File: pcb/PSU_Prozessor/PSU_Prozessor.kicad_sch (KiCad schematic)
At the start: 88 parts, among them IC1 6N138S, J1 ACJS-MHOP, J2 Conn_01x06, J3 FC68148S, J4 USB2066-05-RBHM-15-STB-00-01-A, J7 USB2066-05-RBHM-15-STB-00-01-A, Q1 BC847, Q2 2N7002, Q3 BC847, Q4 2N7002, Q5 BC847, Q6 2N7002, U1 TL072, U2 TL072

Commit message: New version with smaller enclosure
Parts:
- removed C23, C24, C27: 100n, Capacitor_SMD:C_1206_3216Metric_Pad1.33x1.80mm_HandSolder, symbol Device:C
- removed C25, C7: 1u, Capacitor_SMD:C_1206_3216Metric_Pad1.33x1.80mm_HandSolder, symbol Device:C
- removed H4, H5: MountingHole, KiCad_Libs:MountingHole_4mm, symbol Mechanical:MountingHole
- removed J4, J7: USB2066-05-RBHM-15-STB-00-01-A, SamacSys_Parts:USB206605RBHM15STB0001A, symbol SamacSys_Parts:USB2066-05-RBHM-15-STB-00-01-A
- removed J_Swtich_Lower2, J_Swtich_Upper2: Conn_01x08, Connector_JST:JST_PH_B8B-PH-K_1x08_P2.00mm_Vertical, symbol Connector_Generic:Conn_01x08
- removed Q3, Q5: BC847, Package_TO_SOT_SMD:SOT-23, symbol Transistor_BJT:BC847
- removed Q4, Q6: 2N7002, Package_TO_SOT_SMD:SOT-23, symbol Transistor_FET:2N7002
- removed R16, R6: 33k, Resistor_SMD:R_1206_3216Metric_Pad1.30x1.75mm_HandSolder, symbol Device:R
- removed R17, R7: 330, Resistor_SMD:R_1206_3216Metric_Pad1.30x1.75mm_HandSolder, symbol Device:R
- removed R18, R8: 10k, Resistor_SMD:R_1206_3216Metric_Pad1.30x1.75mm_HandSolder, symbol Device:R
- removed R21, R22, R23, R24: 0, Resistor_SMD:R_1206_3216Metric_Pad1.30x1.75mm_HandSolder, symbol Device:R
- removed U2: TL072, SamacSys_Parts:SOIC127P600X175-8N, symbol Amplifier_Operational:TL072
- removed XA1: Arduino_Due_Shield, Arduino:Arduino_Due_Shield, symbol arduino:Arduino_Due_Shield
- added C19: 100n, Capacitor_SMD:C_1206_3216Metric_Pad1.33x1.80mm_HandSolder, symbol Device:C
- added H3: MountingHole, KiCad_Libs:MountingHole_4mm, symbol Mechanical:MountingHole
- added XA1: Arduino_Nano_Socket, Arduino:Arduino_Nano_Socket, symbol arduino:Arduino_Nano_Socket
- renumbered C8 to C1, C21 to C10, C22 to C11, C16 to C12, C14 to C13, C17 to C14, C18 to C16, C19 to C17, C26 to C18, C10 to C2, C2 to C21, C3 to C22, C1 to C23, C12 to C3, C9 to C6, C11 to C7, C13 to C8, C6 to C9, H3 to H2, J3 to J1, J1 to J3, R19 to R1, R9 to R10, R1 to R12, R4 to R13, R2 to R14, R20 to R2, R14 to R3, R5 to R4, R12 to R5, R13 to R6, R15 to R7, R10 to R8, R3 to R9
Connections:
- net INT_Matrix is gone; now on net INT_Status: J_Main_Data1.10 (Pin_10)
- net RCLK_Lower is gone; now on net I2C_Reset: J_Swtich_Lower1.2 (Pin_2)
- net RCLK_Upper is gone; now on net I2C_Reset: J_Swtich_Upper1.2 (Pin_2)
- net SER_Lower is gone; now on net SCL: J_Swtich_Lower1.5 (Pin_5)
- net SER_Upper is gone; now on net SCL: J_Swtich_Upper1.5 (Pin_5)
- net SRCLK_Lower is gone; now on net SDA: J_Swtich_Lower1.4 (Pin_4)
- net SRCLK_Upper is gone; now on net SDA: J_Swtich_Upper1.4 (Pin_4)
- net SRCLR_Upper is gone; now on net INT_Switch: J_Swtich_Upper1.3 (Pin_3)
- net Vref_status is gone; now on net Vref_bl: J_Status1.6 (Pin_6)
- net CS_Amp_N: now also XA1.D6
- net CS_Display: now also XA1.D10 (D10_CS)
- net CS_Fram: now also XA1.D9
- net Expr_1: now also XA1.A0
- net Expr_2: now also XA1.A1
- net GND: now also U1.5 (+), C19.2, XA1.GND1 (GND), XA1.GND2 (GND)
- net I2C_Reset: now also XA1.D5
- net ID_Select_Display: now also XA1.D8
- net INT_Status: now also XA1.D3 (D3_INT1)
- net MISO: now also XA1.D12 (D12_MISO)
- net MOSI: now also J_Main_Data1.6 (Pin_6), XA1.D11 (D11_MOSI)
- net MidiIn: now also XA1.D0 (D0_RX0)
- net MidiOut: now also XA1.D1 (D1_TX0)
- net RCLK_MATRIX: now also XA1.A2
- net Reset_Display: now also XA1.D7
- net SCK: now also J_Main_Data1.7 (Pin_7), XA1.D13 (D13_SCK)
- net SCL: now also XA1.A5 (A5_SCL)
- net SDA: now also XA1.A4 (A4_SDA)
- net SEL_Matrix: now also XA1.A3
- net SW_Ext1: now also XA1.A6
- net SW_Ext2: now also XA1.A7
- net VDD3V3: now also XA1.AREF
- net VDD9V0: now also XA1.VIN
- net Vref_bl: now also J_Swtich_Lower1.6 (Pin_6), J_Swtich_Upper1.6 (Pin_6)
- net Vref_bl_pwm: now also XA1.D4
- net at U1.6 (-): now also U1.7
- net EN_SPL_Matrix: no longer names the net of J_Main_Data1.3 (Pin_3)
- net SRCLR_Lower renamed INT_Switch
- net INT_Switch: now also C19.1, XA1.D2 (D2_INT0)
- removed net Vref_ge: J_Swtich_Lower1.6 (Pin_6), J_Swtich_Upper1.6 (Pin_6), U1.7
- no-connect marks 56 -> 20

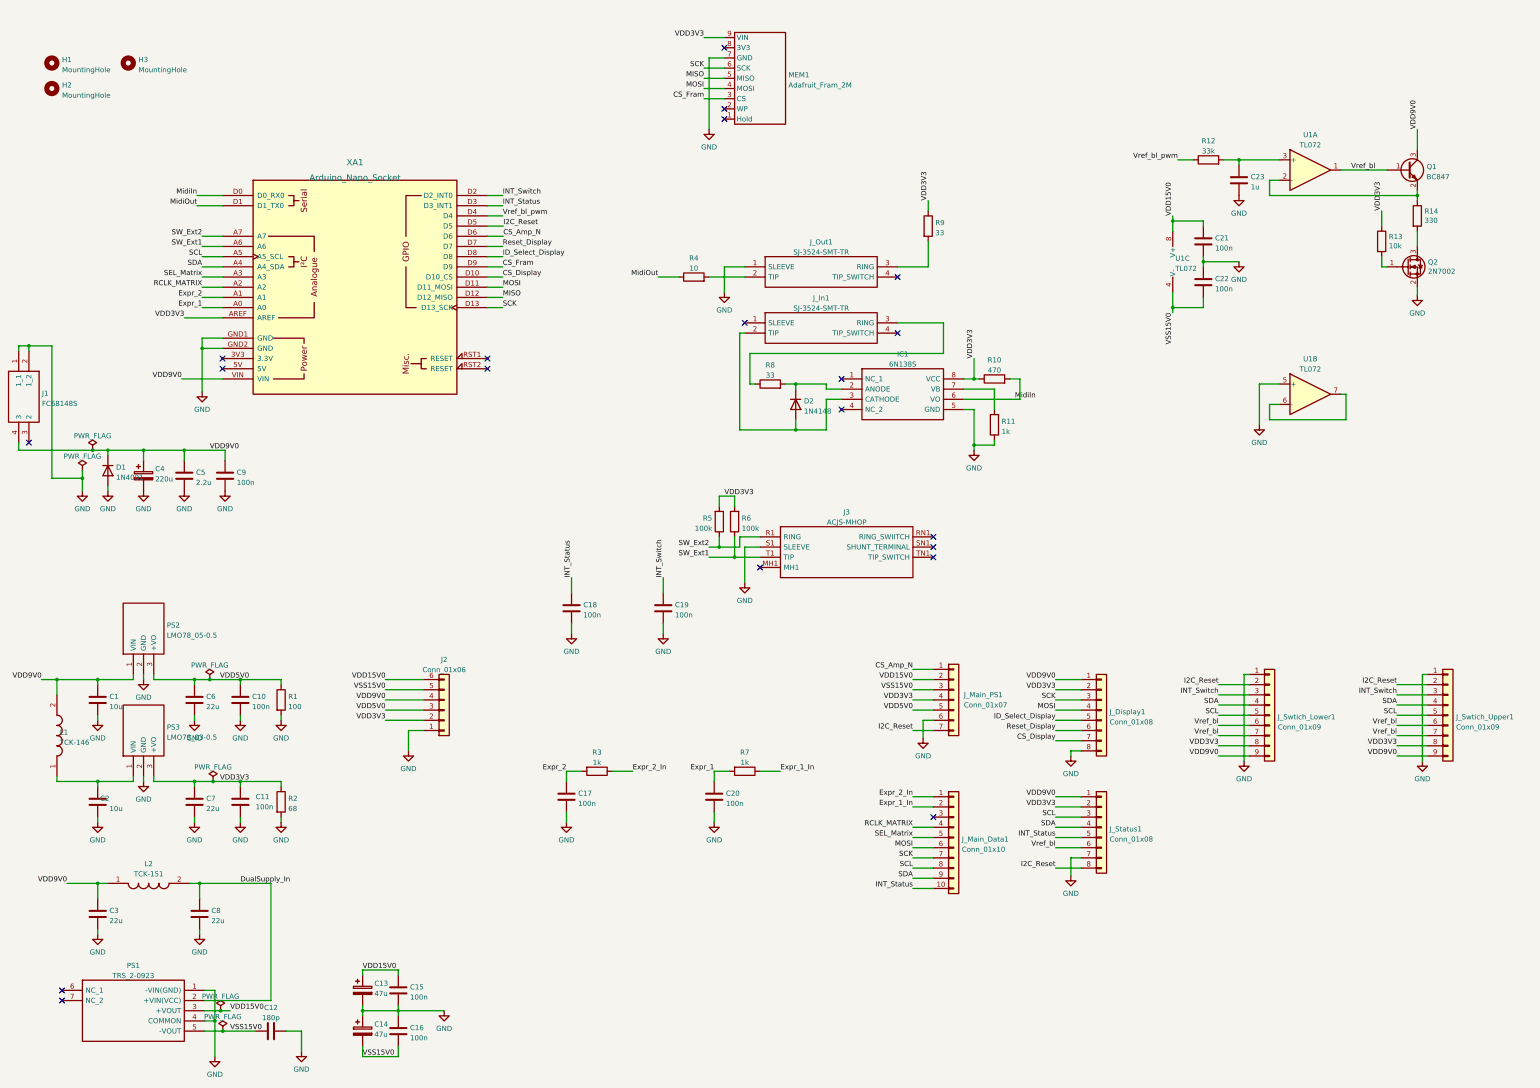
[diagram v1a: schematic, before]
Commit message: All drill holes added
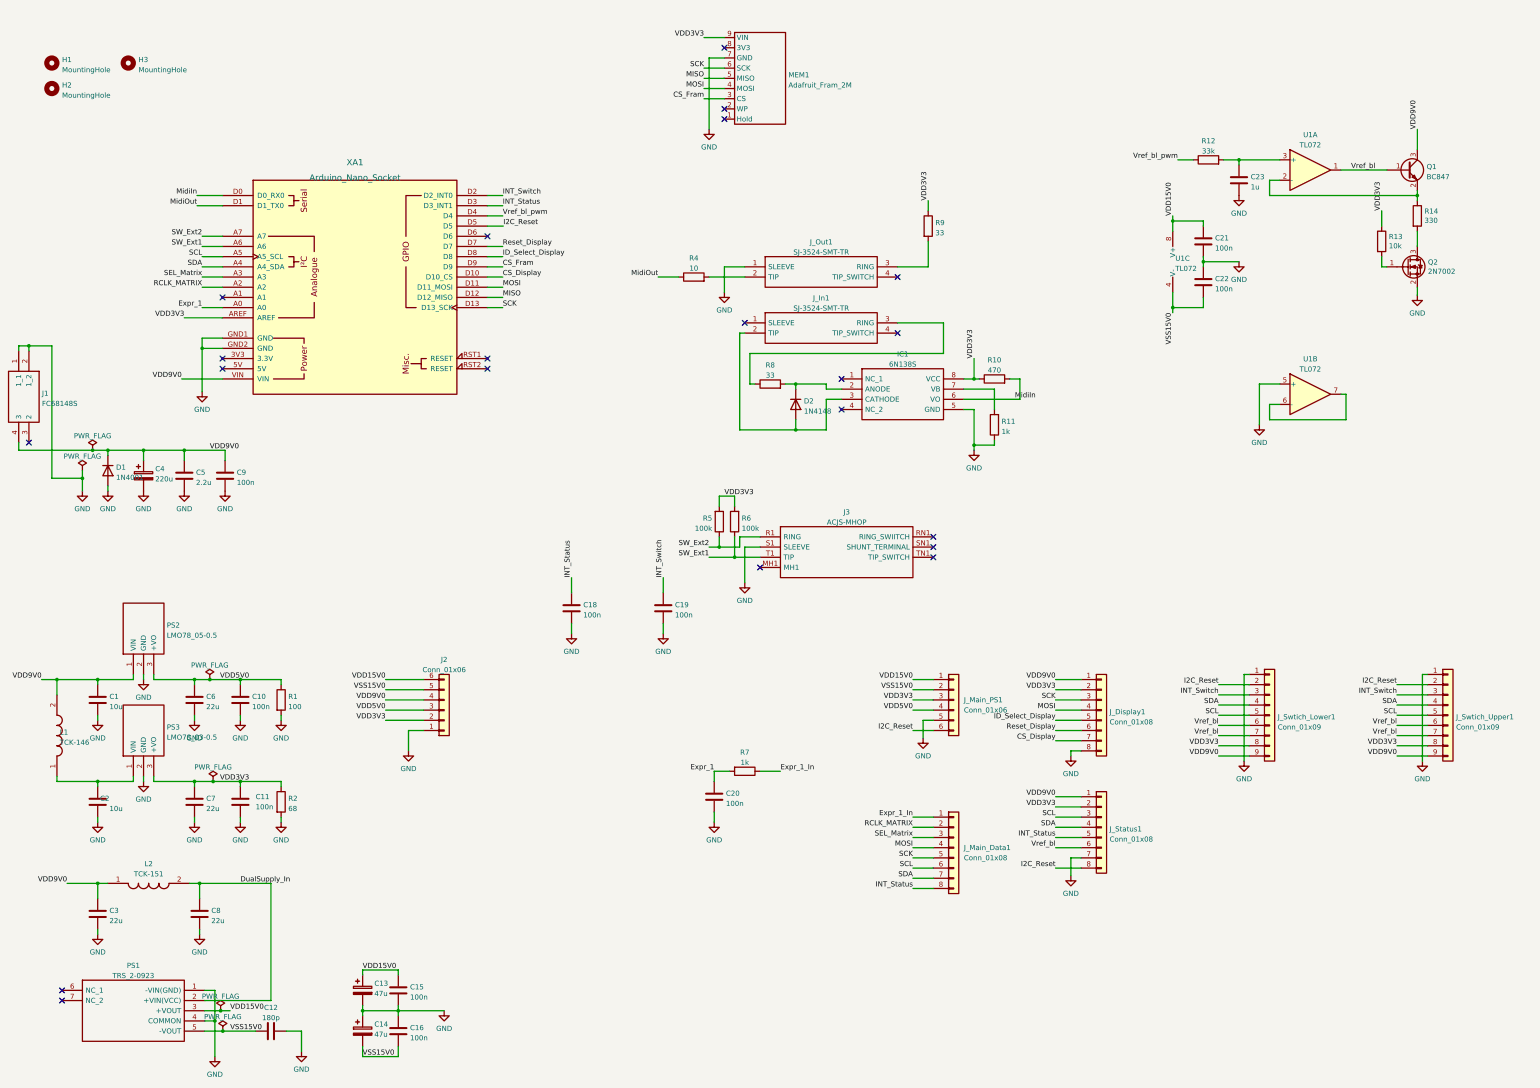
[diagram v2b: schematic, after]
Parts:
- removed C17: 100n, Capacitor_SMD:C_1206_3216Metric_Pad1.33x1.80mm_HandSolder, symbol Device:C
- removed J_Main_Data1: Conn_01x10, Connector_JST:JST_PH_B10B-PH-K_1x10_P2.00mm_Vertical, symbol Connector_Generic:Conn_01x10
- removed J_Main_PS1: Conn_01x07, Connector_JST:JST_PH_B7B-PH-K_1x07_P2.00mm_Vertical, symbol Connector_Generic:Conn_01x07
- removed R3: 1k, Resistor_SMD:R_1206_3216Metric_Pad1.30x1.75mm_HandSolder, symbol Device:R
- added J_Main_Data1: Conn_01x08, Connector_JST:JST_PH_B8B-PH-K_1x08_P2.00mm_Vertical, symbol Connector_Generic:Conn_01x08
- added J_Main_PS1: Conn_01x06, Connector_JST:JST_PH_B6B-PH-K_1x06_P2.00mm_Vertical, symbol Connector_Generic:Conn_01x06
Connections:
- net Expr_1_In: now also J_Main_Data1.1 (Pin_1)
- net GND: now also J_Main_PS1.5 (Pin_5)
- net I2C_Reset: now also J_Main_PS1.6 (Pin_6)
- net INT_Status: now also J_Main_Data1.8 (Pin_8)
- net MOSI: now also J_Main_Data1.4 (Pin_4)
- net RCLK_MATRIX: now also J_Main_Data1.2 (Pin_2)
- net SCK: now also J_Main_Data1.5 (Pin_5)
- net SCL: now also J_Main_Data1.6 (Pin_6)
- net SDA: now also J_Main_Data1.7 (Pin_7)
- net SEL_Matrix: now also J_Main_Data1.3 (Pin_3)
- net VDD15V0: now also J_Main_PS1.1 (Pin_1)
- net VDD3V3: now also J_Main_PS1.3 (Pin_3)
- net VDD5V0: now also J_Main_PS1.4 (Pin_4)
- net VSS15V0: now also J_Main_PS1.2 (Pin_2)
- net CS_Amp_N: no longer names the net of XA1.D6
- net Expr_2: no longer names the net of XA1.A1
- no-connect marks 20 -> 21
